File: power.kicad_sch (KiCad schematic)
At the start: 1 part, among them U4 LT1963AxST-3.3

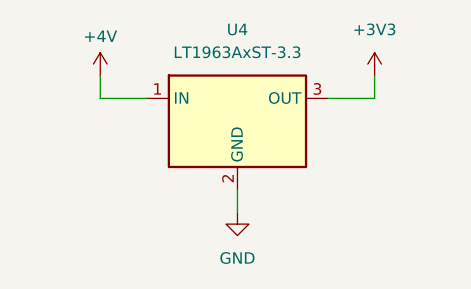
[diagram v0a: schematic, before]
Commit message: Added pull-ups to sdmmc
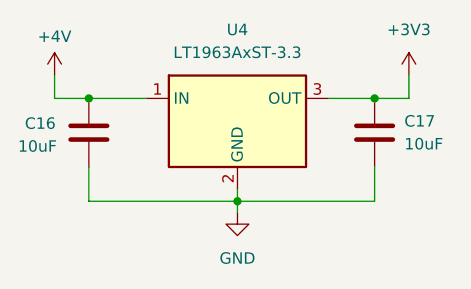
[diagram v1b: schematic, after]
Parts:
- added C16, C17: 10uF, symbol Device:C
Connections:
- net +3V3: now also C17.1
- net +4V: now also C16.1
- net GND: now also C16.2, C17.2

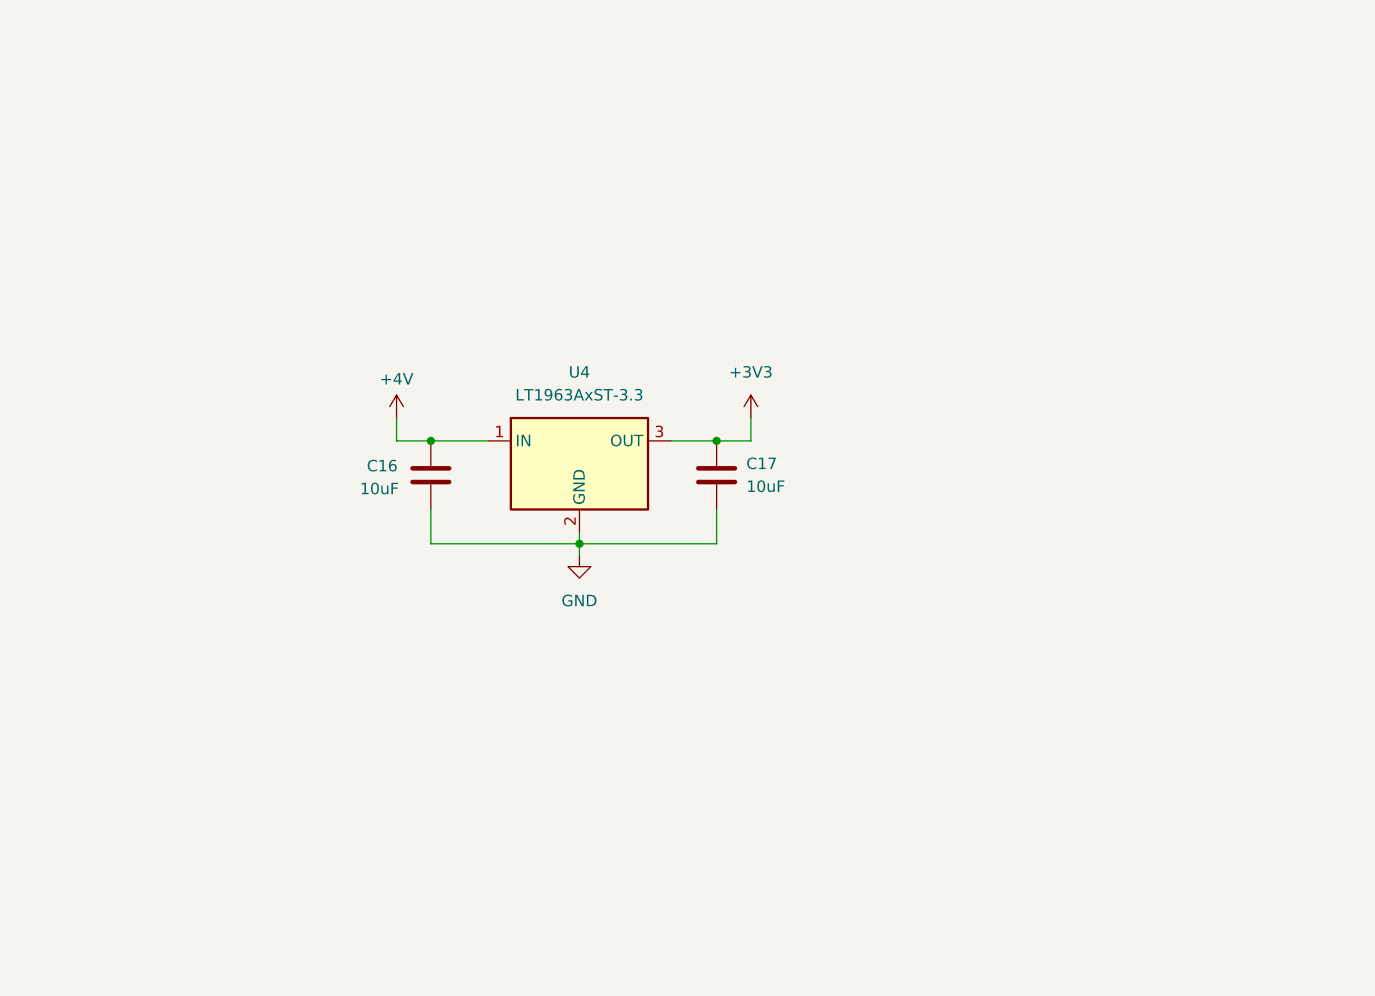
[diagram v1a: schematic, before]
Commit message: Changed PowerSupply idea: use jumper to select PoE or VBUS
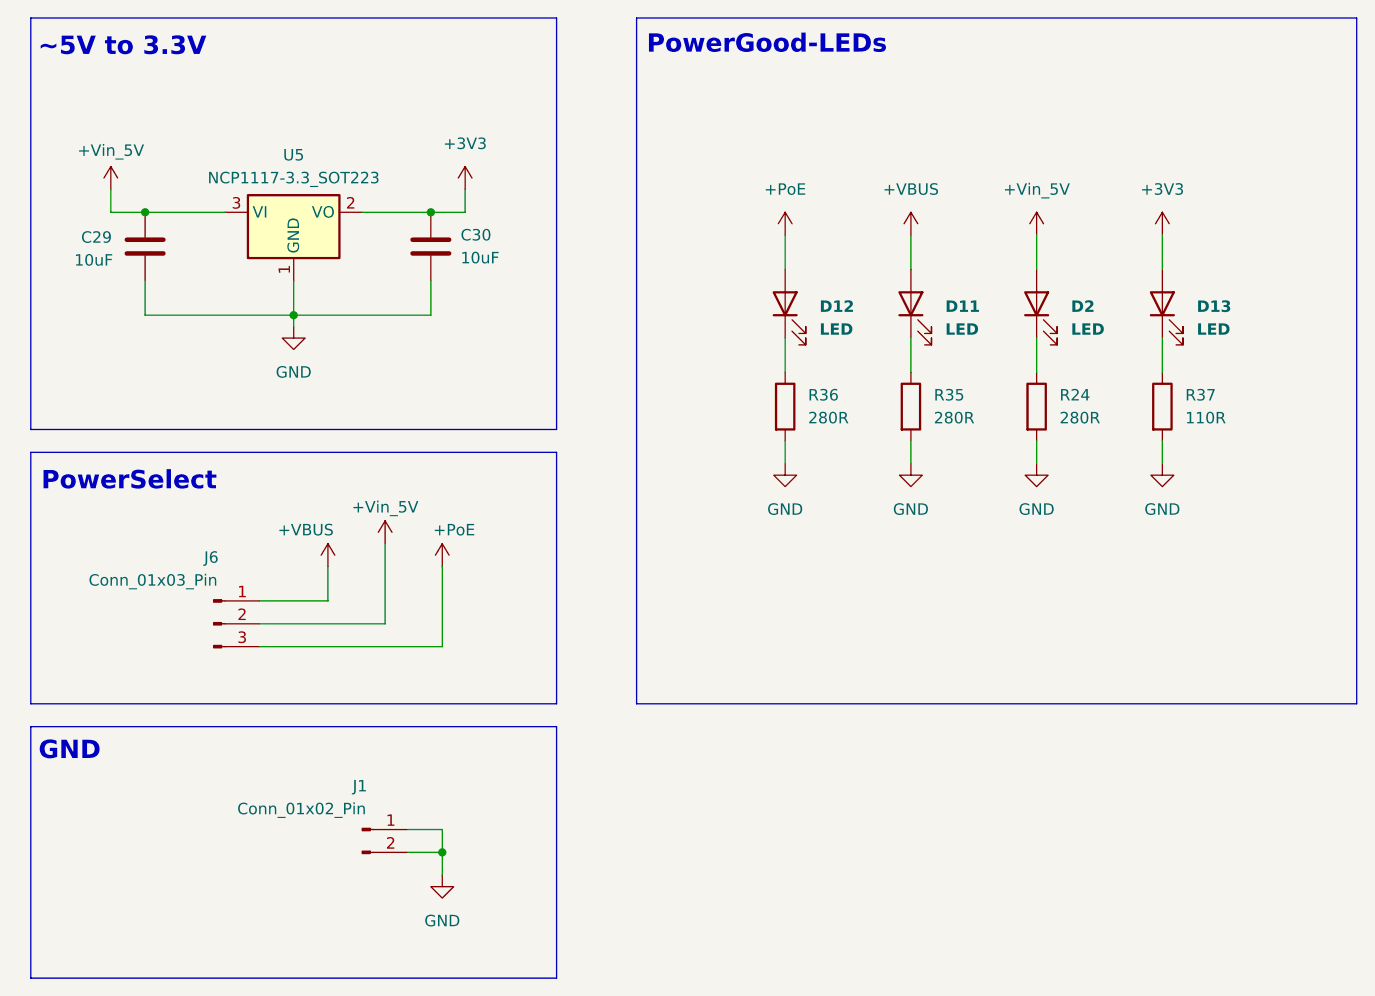
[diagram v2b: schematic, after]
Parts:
- removed C16, C17: 10uF, symbol Device:C
- removed U4: LT1963AxST-3.3, Package_TO_SOT_SMD:SOT-223-3_TabPin2, symbol Regulator_Linear:LT1963AxST-3.3
- added C29, C30: 10uF, Capacitor_SMD:C_0805_2012Metric_Pad1.18x1.45mm_HandSolder, symbol Device:C
- added D11, D12, D13, D2: LED, LED_SMD:LED_0805_2012Metric_Pad1.15x1.40mm_HandSolder, symbol Device:LED
- added J1: Conn_01x02_Pin, Connector_Wire:SolderWire-0.15sqmm_1x02_P4mm_D0.5mm_OD1.5mm, symbol Connector:Conn_01x02_Pin
- added J6: Conn_01x03_Pin, Connector_Wire:SolderWire-0.15sqmm_1x03_P4mm_D0.5mm_OD1.5mm, symbol Connector:Conn_01x03_Pin
- added R24, R35, R36: 280R, Resistor_SMD:R_0805_2012Metric_Pad1.20x1.40mm_HandSolder, symbol Device:R
- added R37: 110R, Resistor_SMD:R_0805_2012Metric_Pad1.20x1.40mm_HandSolder, symbol Device:R
- added U5: NCP1117-3.3_SOT223, Package_TO_SOT_SMD:SOT-223-3_TabPin2, symbol Regulator_Linear:NCP1117-3.3_SOT223
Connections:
- net +3V3: now also C30.1, D13.2 (A), U5.2 (VO)
- net GND: now also C29.2, C30.2, J1.1 (Pin_1), J1.2 (Pin_2), R24.2, R35.2, R36.2, R37.2, U5.1 (GND)
- new net: D12.1 (K), R36.1
- new net: D13.1 (K), R37.1
- new net: D2.1 (K), R24.1
- new net: D11.1 (K), R35.1
- new net +PoE: D12.2 (A), J6.3 (Pin_3)
- new net +VBUS: D11.2 (A), J6.1 (Pin_1)
- new net +Vin_5V: C29.1, D2.2 (A), J6.2 (Pin_2), U5.3 (VI)
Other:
- note added: "GND"
- note added: "PowerGood-LEDs"
- note added: "PowerSelect"
- note added: "~5V to 3.3V"

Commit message: Started layout v2
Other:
- moved on the sheet: J1
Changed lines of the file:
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@@
 	)
 	(junction
-		(at 66.04 111.76)
+		(at 50.8 111.76)
 		(diameter 0)
 		(color 0 0 0 1)
@@
 	(wire
 		(pts
-			(xy 66.04 111.76) (xy 66.04 114.3)
+			(xy 50.8 111.76) (xy 50.8 114.3)
 		)
 		(stroke
@@
 	(wire
 		(pts
-			(xy 62.23 109.22) (xy 66.04 109.22)
+			(xy 46.99 109.22) (xy 50.8 109.22)
 		)
 		(stroke
@@
 	(wire
 		(pts
-			(xy 62.23 111.76) (xy 66.04 111.76)
+			(xy 46.99 111.76) (xy 50.8 111.76)
 		)
 		(stroke
@@
 	(wire
 		(pts
-			(xy 66.04 109.22) (xy 66.04 111.76)
+			(xy 50.8 109.22) (xy 50.8 111.76)
 		)
 		(stroke
@@
 	(symbol
 		(lib_id "Connector:Conn_01x02_Pin")
-		(at 57.15 109.22 0)
+		(at 41.91 109.22 0)
 		(unit 1)
 		(exclude_from_sim no)
@@
 		(dnp no)
 		(property "Reference" "J1"
-			(at 56.896 104.394 0)
+			(at 41.656 104.394 0)
 			(effects
 				(font
@@
 		)
 		(property "Value" "Conn_01x02_Pin"
-			(at 50.419 106.934 0)
+			(at 35.179 106.934 0)
 			(effects
 				(font
@@
 		)
 		(property "Footprint" "Connector_Wire:SolderWire-0.15sqmm_1x02_P4mm_D0.5mm_OD1.5mm"
-			(at 57.15 109.22 0)
+			(at 41.91 109.22 0)
 			(effects
 				(font
@@
 		)
 		(property "Datasheet" "~"
-			(at 57.15 109.22 0)
+			(at 41.91 109.22 0)
 			(effects
 				(font
@@
 		)
 		(property "Description" "Generic connector, single row, 01x02, script generated"
-			(at 57.15 109.22 0)
+			(at 41.91 109.22 0)
 			(effects
 				(font
@@
 	(symbol
 		(lib_id "power:GND")
-		(at 66.04 114.3 0)
+		(at 50.8 114.3 0)
 		(unit 1)
 		(exclude_from_sim no)
@@
 		(fields_autoplaced yes)
 		(property "Reference" "#PWR037"
-			(at 66.04 120.65 0)
+			(at 50.8 120.65 0)
 			(effects
 				(font
@@
 		)
 		(property "Value" "GND"
-			(at 66.04 119.38 0)
+			(at 50.8 119.38 0)
 			(effects
 				(font
@@
 		)
 		(property "Footprint" ""
-			(at 66.04 114.3 0)
+			(at 50.8 114.3 0)
 			(effects
 				(font
@@
 		)
 		(property "Datasheet" ""
-			(at 66.04 114.3 0)
+			(at 50.8 114.3 0)
 			(effects
 				(font
@@
 		)
 		(property "Description" "Power symbol creates a global label with name \"GND\" , ground"
-			(at 66.04 114.3 0)
-			(effects
-				(font
+			(at 50.8 114.3 0)
+			(effects
+				(font
